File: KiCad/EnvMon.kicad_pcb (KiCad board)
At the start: 2 copper layers, 44.5 x 37 mm, 17 parts, among them J1 USB-C, J2 DC, J3 GPIO, M1 D24V5F3-NoSHDN, M2 OLED1.5-RGB, M3 SCD30-4pin, U1 FT230XQ, U2 ESP32-WROOM-32

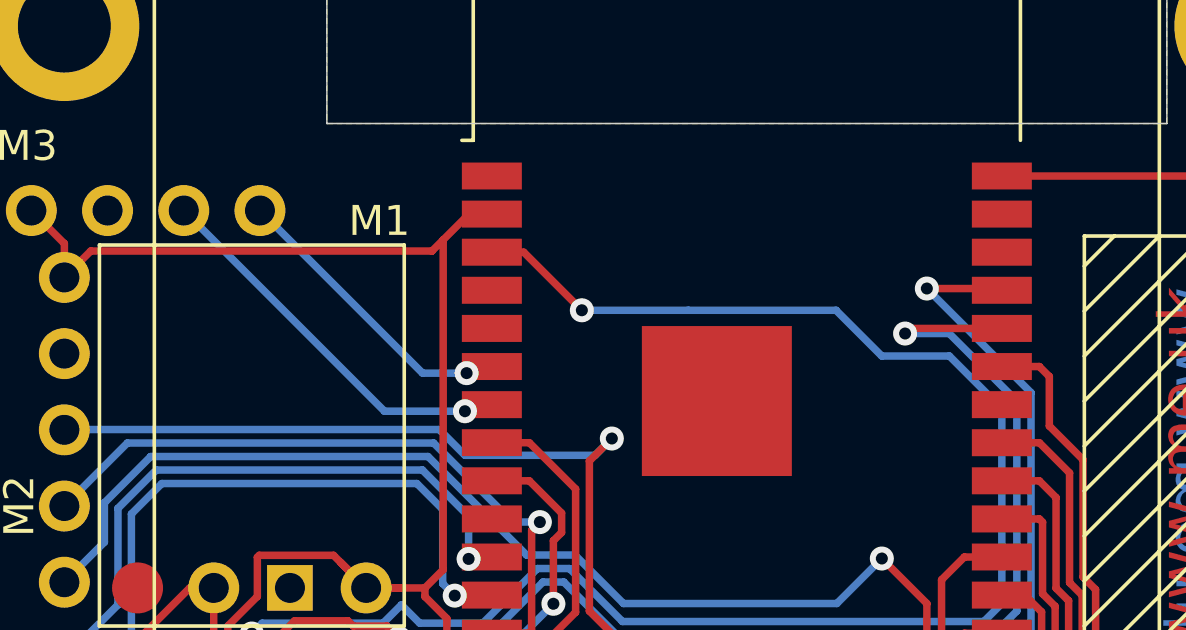
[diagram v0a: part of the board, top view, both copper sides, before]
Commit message: Moved CO2 to usable GPIOs
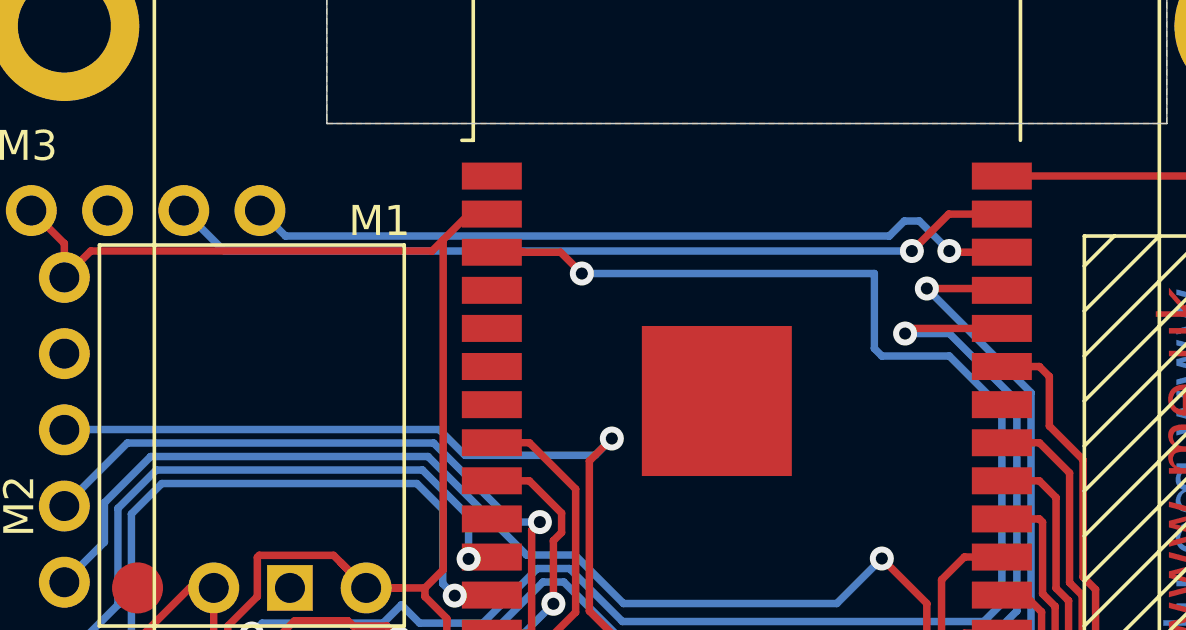
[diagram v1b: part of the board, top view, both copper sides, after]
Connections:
- U2 pad 36: Net-(U2-Pad36) -> CO2-SDA
- U2 pad 37: Net-(U2-Pad37) -> CO2-SCL
- U2 pad 6: CO2-SDA -> Net-(U2-Pad6)
- U2 pad 7: CO2-SCL -> Net-(U2-Pad7)
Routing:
- net CO2-SDA: track 10.1 -> 25.7 mm
- net CO2-SCL: track 13.1 -> 28.3 mm
- net Net-(U1-Pad16): track 53.8 -> 56.3 mm

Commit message: Tidy
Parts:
- added R10: 27R, Resistor_SMD:R_1206_3216Metric_Pad1.30x1.75mm_HandSolder, B.Cu at (107.8, 105.2)
- added R11: 27R, Resistor_SMD:R_1206_3216Metric_Pad1.30x1.75mm_HandSolder, B.Cu at (104.5, 105.2)
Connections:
- U1 pad 7: Net-(J1-PadA7) -> Net-(R10-Pad1)
- U1 pad 9: +3V3 -> Net-(R11-Pad1)

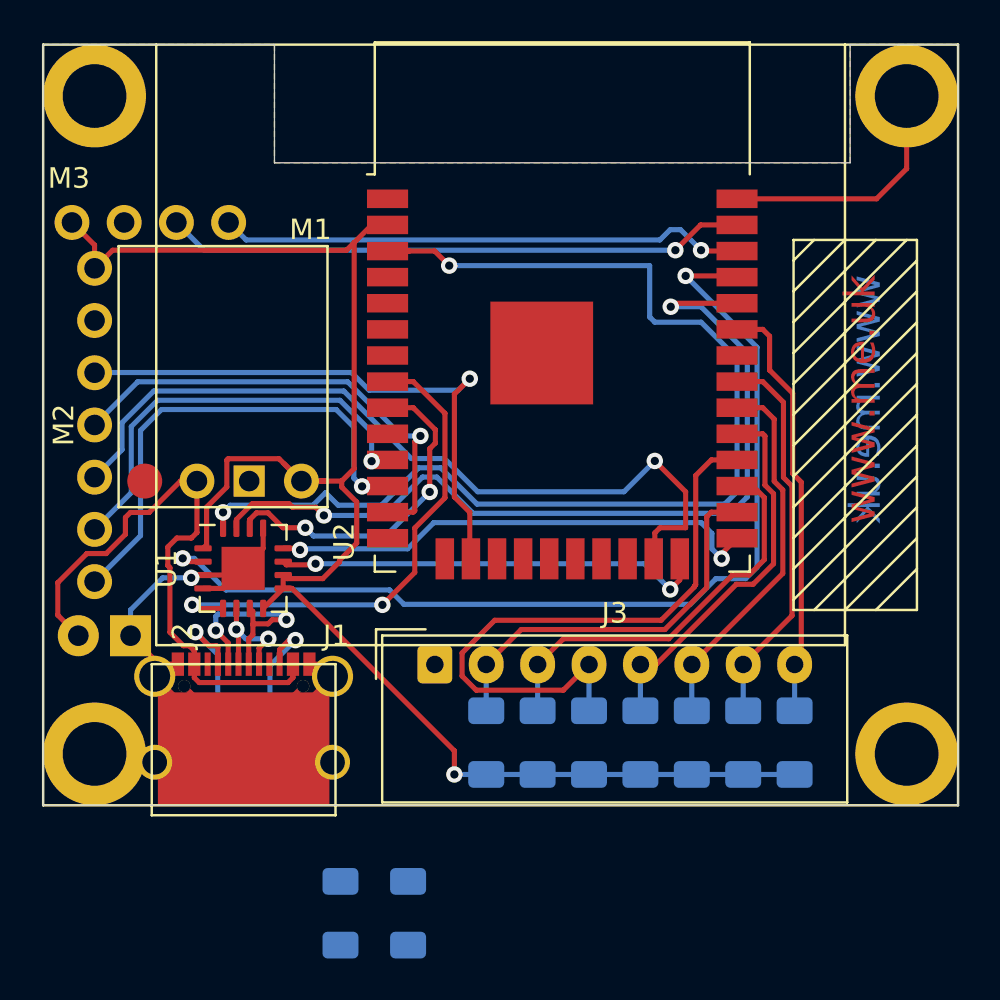
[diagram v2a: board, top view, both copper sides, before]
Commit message: Started on SPI logic now
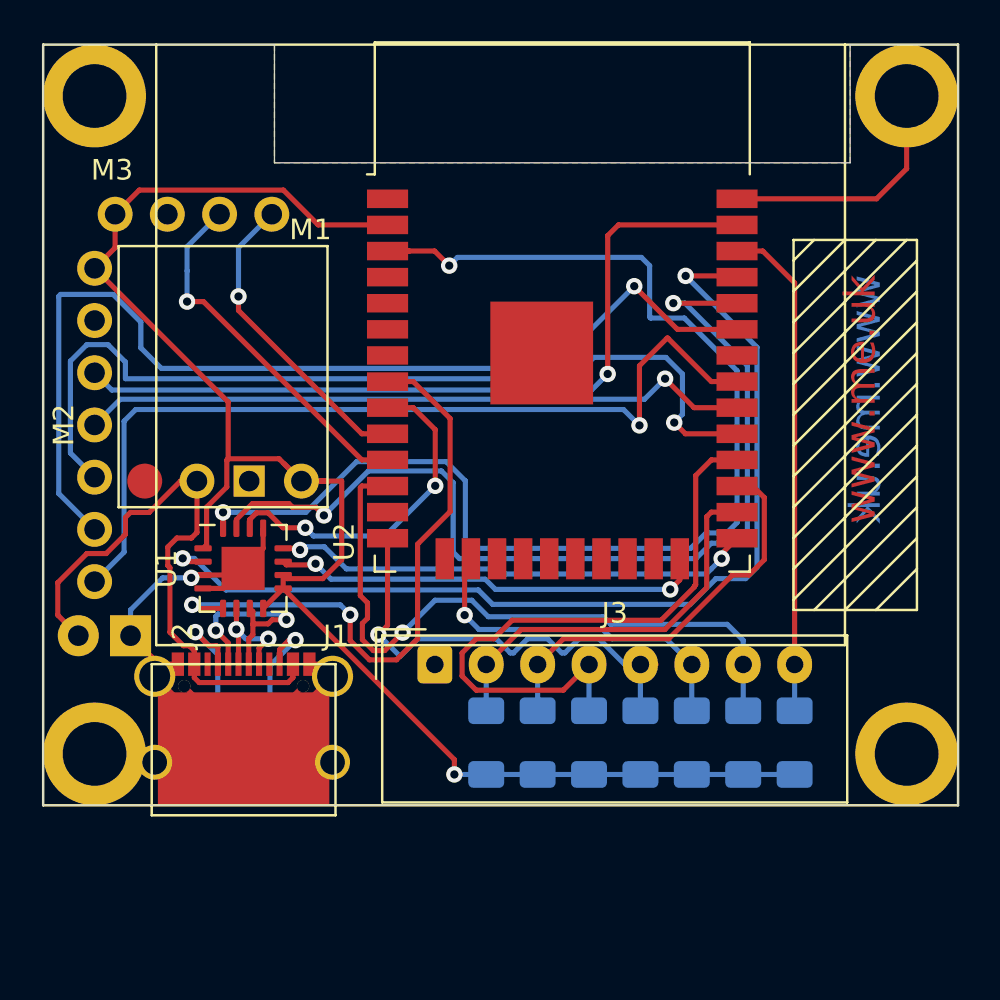
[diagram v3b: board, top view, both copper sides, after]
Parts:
- removed R10, R11: 27R, Resistor_SMD:R_1206_3216Metric_Pad1.30x1.75mm_HandSolder
- moved M3 2.14 mm to (127.1, 69.8)
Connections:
- U1 pad 7: Net-(R10-Pad1) -> Net-(J1-PadA7)
- U1 pad 9: Net-(R11-Pad1) -> +3V3
- U2 pad 10: Net-(U2-Pad10) -> CO2-SDA
- U2 pad 11: OLED-DC -> CO2-SCL
- U2 pad 12: OLED-RST -> IO6
- U2 pad 13: OLED-SCLK -> Net-(U2-Pad13)
- U2 pad 14: Net-(U2-Pad14) -> IO4
- U2 pad 16: OLED-MOSI -> IO5
- U2 pad 23: OLED-CS0 -> Net-(U2-Pad23)
- U2 pad 29: IO4 -> OLED-CS0
- U2 pad 30: IO5 -> OLED-SCLK
- U2 pad 31: IO6 -> OLED-RST
- U2 pad 33: IO7 -> OLED-DC
- U2 pad 36: CO2-SDA -> IO7
- U2 pad 37: CO2-SCL -> OLED-MOSI
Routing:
- net OLED-DC: track 20.8 -> 49.8 mm
- net OLED-RST: track 23.7 -> 43.1 mm
- net IO6: track 18.8 -> 33.0 mm, vias 0 -> 1
- net CO2-SDA: track 25.7 -> 15.1 mm
- net OLED-MOSI: track 28.2 -> 38.9 mm
- net CO2-SCL: track 28.3 -> 17.8 mm
- net OLED-SCLK: track 22.9 -> 32.8 mm
- net OLED-CS0: track 39.2 -> 44.4 mm
- net CBUS2: track 24.8 -> 30.0 mm
- net Net-(U1-Pad15): track 42.6 -> 47.2 mm
- net IO4: track 18.5 -> 23.1 mm, vias 0 -> 1
- net Net-(U1-Pad16): track 56.3 -> 60.5 mm
- net IO7: track 20.7 -> 24.7 mm
- net +3V3: track 82.0 -> 80.9 mm
- net IO5: track 18.2 -> 17.2 mm, vias 0 -> 1
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
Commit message: Started working
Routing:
- net GND: track 62.0 -> 65.3 mm
- net OLED-RST: track 43.1 -> 41.3 mm
- net OLED-CS0: track 44.4 -> 42.6 mm
- net +3V3: track 80.9 -> 82.4 mm
- net Net-(J1-PadB5): track 5.72 -> 7.20 mm
- net Net-(J1-PadA5): track 6.60 -> 7.88 mm
- net OLED-MOSI: track 38.9 -> 38.3 mm

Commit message: SCAD
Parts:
- moved U2 0.25 mm to (115.2, 79.0)
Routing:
- net IO7: track 24.7 -> 27.8 mm
- net CBUS1: track 21.1 -> 23.0 mm

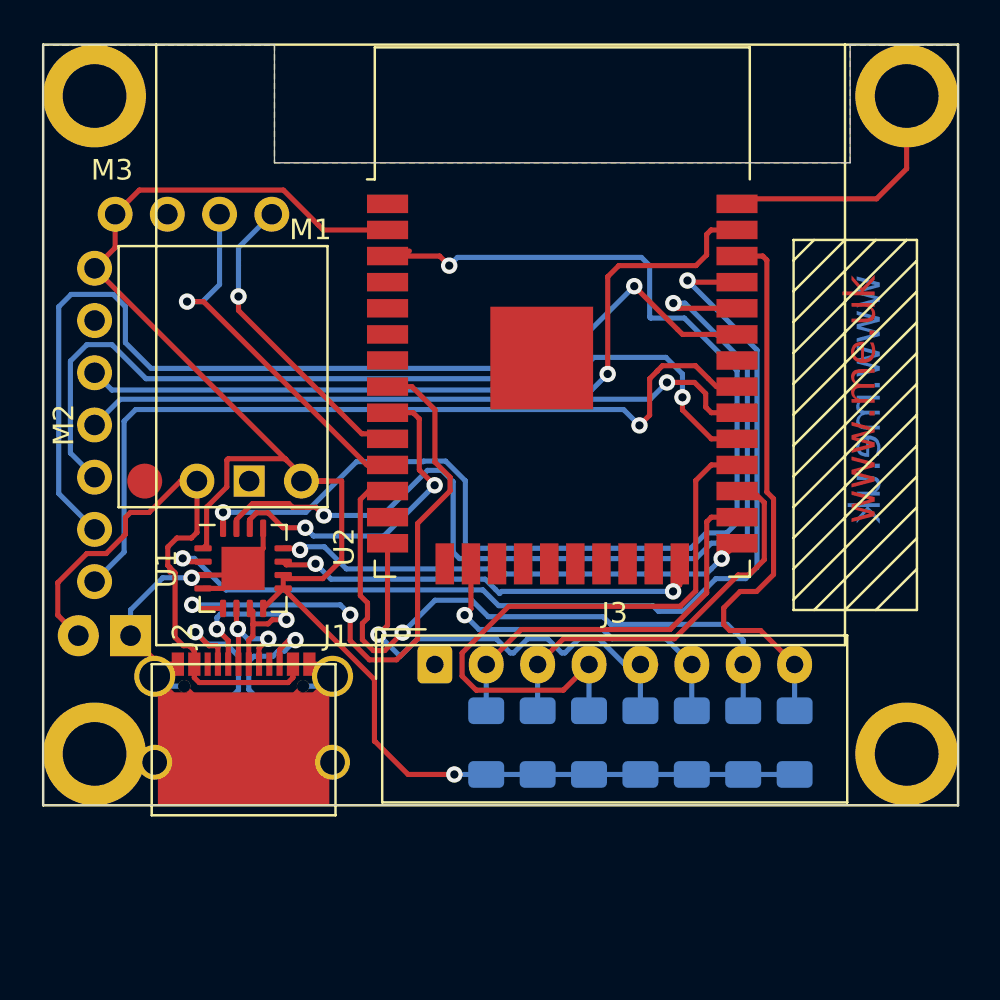
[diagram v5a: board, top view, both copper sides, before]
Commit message: Tidy tracks around FT230X
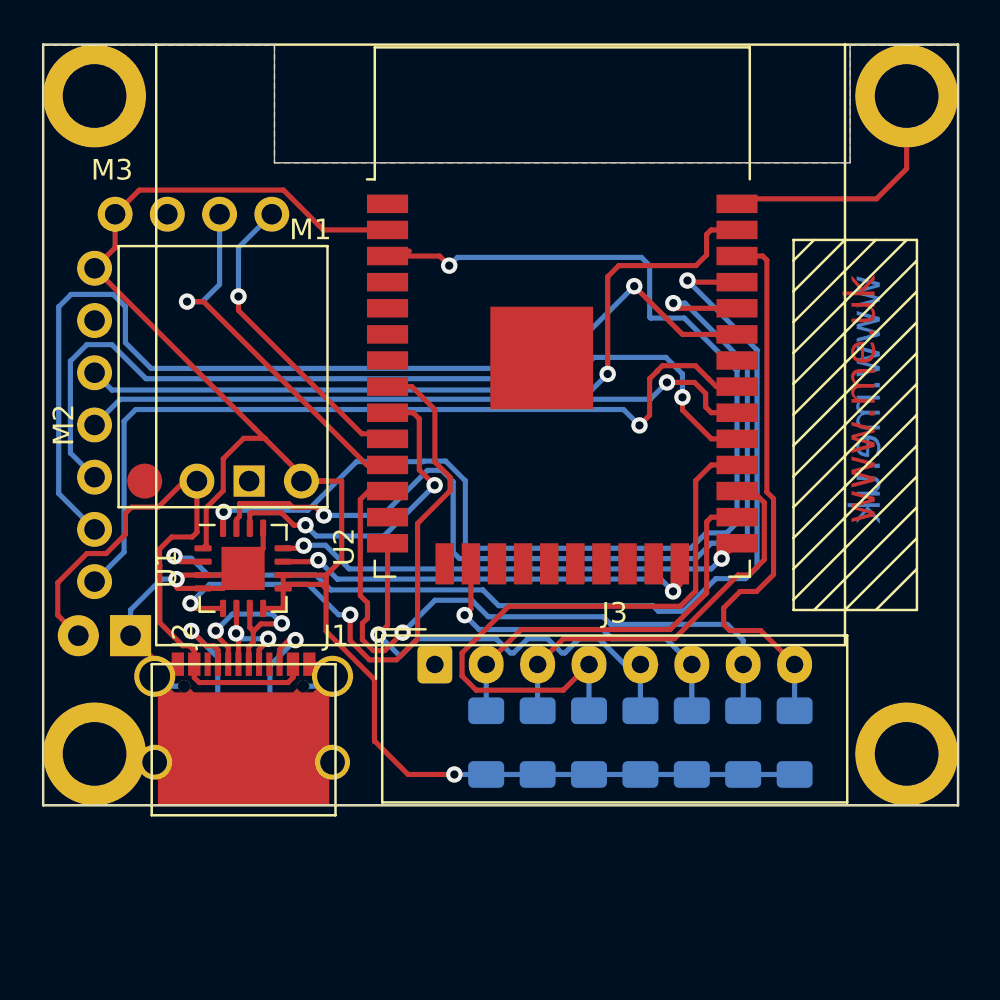
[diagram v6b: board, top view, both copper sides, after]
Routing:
- net +3V3: track 82.5 -> 84.5 mm
- net GND: track 65.3 -> 67.0 mm
- net Net-(J1-PadB5): track 7.20 -> 5.62 mm
- net Net-(U1-Pad2): track 48.7 -> 50.1 mm
- net Net-(J1-PadA5): track 7.88 -> 6.78 mm
- net CBUS2: track 29.7 -> 30.7 mm
- net Net-(J1-PadA7): track 10.6 -> 10.0 mm

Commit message: Revised for SCD30 contact
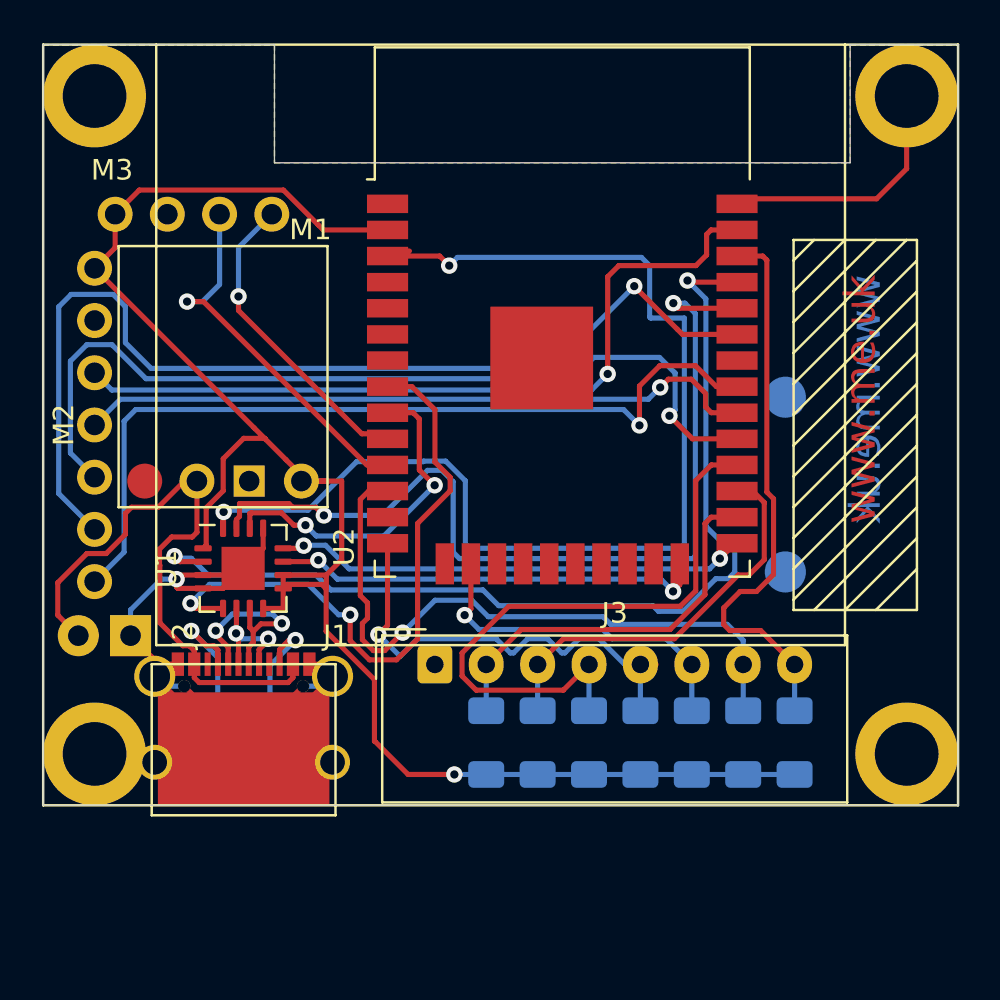
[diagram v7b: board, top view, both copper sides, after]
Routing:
- net Net-(U1-Pad15): track 47.8 -> 44.7 mm
- net Net-(U1-Pad16): track 60.4 -> 57.4 mm
- net Net-(U1-Pad2): track 50.1 -> 48.8 mm
- net OLED-CS0: track 43.1 -> 43.7 mm

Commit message: Tweak for DC
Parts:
- J2: moved to B.Cu
- moved J2 3.18 mm to (91.6, 93.5), turned to 135 degrees
- moved M3 3.13 mm to (130.2, 69.4)
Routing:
- net Net-(J1-PadA4): track 29.8 -> 22.0 mm
- net GND: track 67.0 -> 74.8 mm
- net CO2-SCL: track 18.4 -> 15.2 mm, vias 1 -> 0
- net CO2-SDA: track 15.1 -> 13.2 mm, vias 1 -> 0
- net +3V3: track 84.5 -> 83.3 mm, vias 1 -> 2
- net Net-(U1-Pad16): track 57.4 -> 56.4 mm
